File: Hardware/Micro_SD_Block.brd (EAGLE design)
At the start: 30.5 x 44.5 mm, 16 parts, among them U1 USD-SOCKETNEW, U2 EDISON_CONNECTOR_FULLMOUNTING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, U3 EDISON_CONNECTOR_FULLHEADER

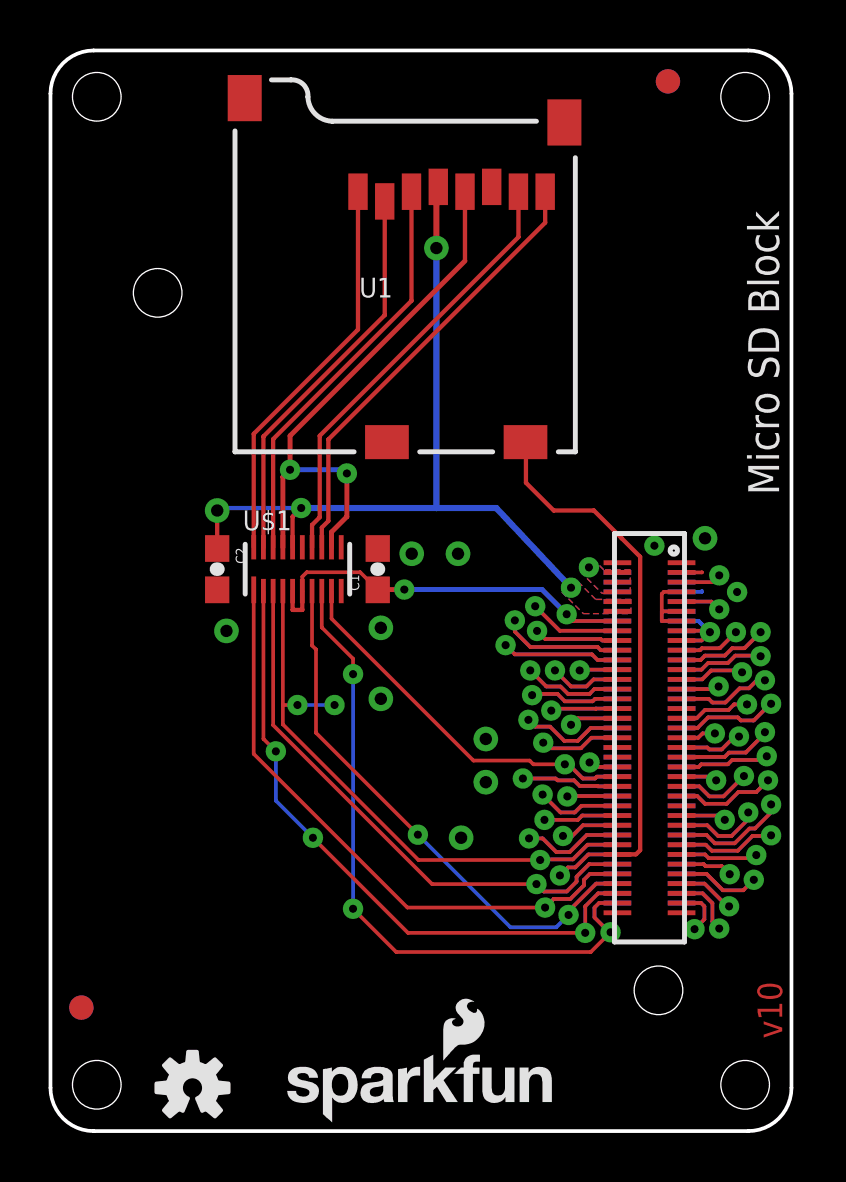
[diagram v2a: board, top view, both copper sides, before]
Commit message: Moved 3.3v bus out from under highspeed lines updated edison connector footprint to remove jumpers removed jumpers from txb0108
TODO: Remove P$#'s from txb0108 in library
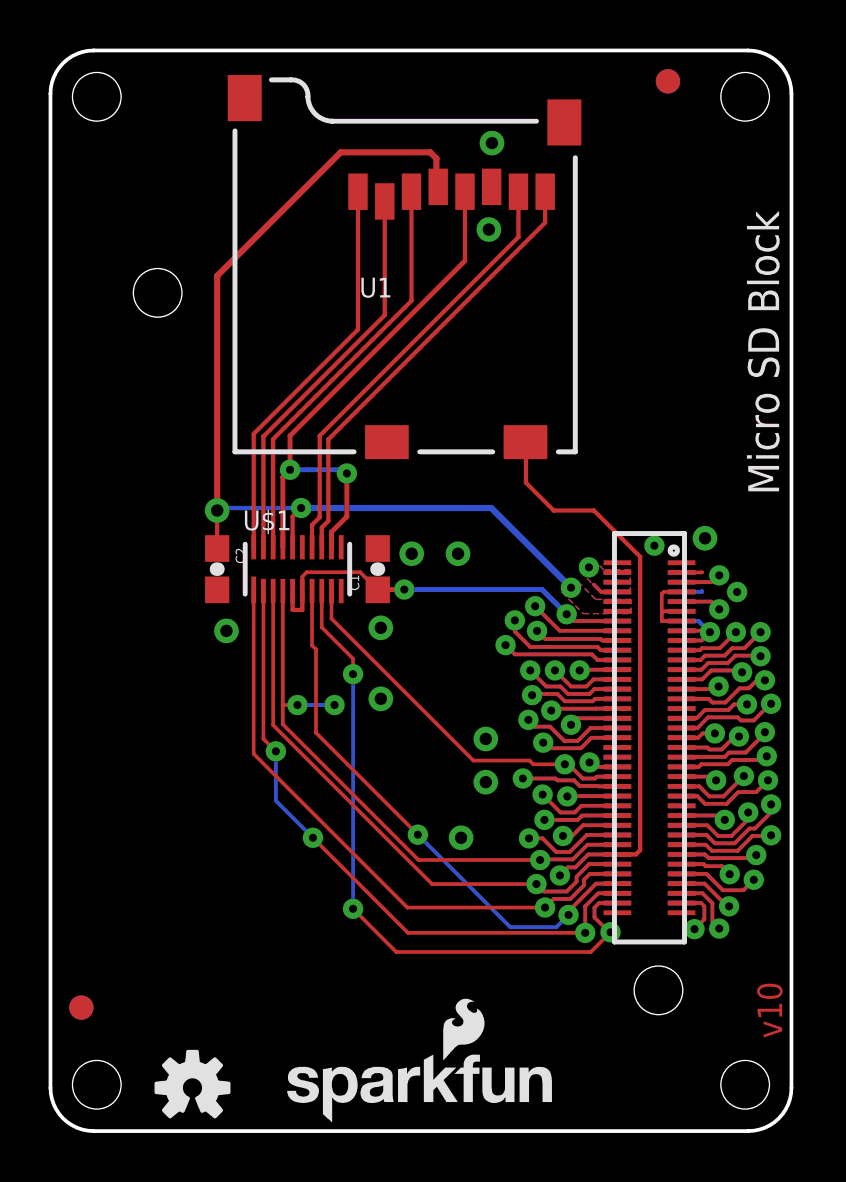
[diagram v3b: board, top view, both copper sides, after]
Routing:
- net 3.3V: track 32.6 -> 41.5 mm, vias 4 -> 3
- net VSYS: track 0.00 -> 2.18 mm
- net GND: vias 12 -> 14
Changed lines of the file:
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@@
 <layers>
 <layer number="1" name="Top" color="4" fill="1" visible="yes" active="yes"/>
-<layer number="2" name="Route2" color="1" fill="3" visible="yes" active="yes"/>
-<layer number="15" name="Route15" color="4" fill="6" visible="yes" active="yes"/>
+<layer number="2" name="Route2" color="1" fill="3" visible="no" active="yes"/>
+<layer number="15" name="Route15" color="4" fill="6" visible="no" active="yes"/>
 <layer number="16" name="Bottom" color="1" fill="1" visible="yes" active="yes"/>
 <layer number="17" name="Pads" color="2" fill="1" visible="yes" active="yes"/>
@@
 <layer number="21" name="tPlace" color="16" fill="1" visible="yes" active="yes"/>
 <layer number="22" name="bPlace" color="14" fill="1" visible="yes" active="yes"/>
-<layer number="23" name="tOrigins" color="15" fill="1" visible="yes" active="yes"/>
-<layer number="24" name="bOrigins" color="15" fill="1" visible="yes" active="yes"/>
-<layer number="25" name="tNames" color="7" fill="1" visible="yes" active="yes"/>
-<layer number="26" name="bNames" color="7" fill="1" visible="yes" active="yes"/>
-<layer number="27" name="tValues" color="7" fill="1" visible="yes" active="yes"/>
-<layer number="28" name="bValues" color="7" fill="1" visible="yes" active="yes"/>
-<layer number="29" name="tStop" color="7" fill="3" visible="yes" active="yes"/>
-<layer number="30" name="bStop" color="7" fill="6" visible="yes" active="yes"/>
-<layer number="31" name="tCream" color="7" fill="4" visible="yes" active="yes"/>
-<layer number="32" name="bCream" color="7" fill="5" visible="yes" active="yes"/>
-<layer number="39" name="tKeepout" color="4" fill="11" visible="yes" active="yes"/>
-<layer number="40" name="bKeepout" color="1" fill="11" visible="yes" active="yes"/>
-<layer number="41" name="tRestrict" color="4" fill="10" visible="yes" active="yes"/>
-<layer number="42" name="bRestrict" color="1" fill="10" visible="yes" active="yes"/>
-<layer number="43" name="vRestrict" color="2" fill="10" visible="yes" active="yes"/>
-<layer number="44" name="Drills" color="7" fill="1" visible="yes" active="yes"/>
-<layer number="45" name="Holes" color="7" fill="1" visible="yes" active="yes"/>
-<layer number="46" name="Milling" color="3" fill="1" visible="yes" active="yes"/>
-<layer number="51" name="tDocu" color="6" fill="1" visible="yes" active="yes"/>
+<layer number="23" name="tOrigins" color="15" fill="1" visible="no" active="yes"/>
+<layer number="24" name="bOrigins" color="15" fill="1" visible="no" active="yes"/>
+<layer number="25" name="tNames" color="7" fill="1" visible="no" active="yes"/>
+<layer number="26" name="bNames" color="7" fill="1" visible="no" active="yes"/>
+<layer number="27" name="tValues" color="7" fill="1" visible="no" active="yes"/>
+<layer number="28" name="bValues" color="7" fill="1" visible="no" active="yes"/>
+<layer number="29" name="tStop" color="7" fill="3" visible="no" active="yes"/>
+<layer number="30" name="bStop" color="7" fill="6" visible="no" active="yes"/>
+<layer number="31" name="tCream" color="7" fill="4" visible="no" active="yes"/>
+<layer number="32" name="bCream" color="7" fill="5" visible="no" active="yes"/>
+<layer number="39" name="tKeepout" color="4" fill="11" visible="no" active="yes"/>
+<layer number="40" name="bKeepout" color="1" fill="11" visible="no" active="yes"/>
+<layer number="41" name="tRestrict" color="4" fill="10" visible="no" active="yes"/>
+<layer number="42" name="bRestrict" color="1" fill="10" visible="no" active="yes"/>
+<layer number="43" name="vRestrict" color="2" fill="10" visible="no" active="yes"/>
+<layer number="44" name="Drills" color="7" fill="1" visible="no" active="yes"/>
+<layer number="45" name="Holes" color="7" fill="1" visible="no" active="yes"/>
+<layer number="46" name="Milling" color="3" fill="1" visible="no" active="yes"/>
+<layer number="51" name="tDocu" color="6" fill="1" visible="no" active="yes"/>
 <layer number="3" name="Route3" color="4" fill="3" visible="no" active="no"/>
 <layer number="4" name="Route4" color="1" fill="4" visible="no" active="no"/>
@@
 <layer number="251" name="SMDround" color="12" fill="11" visible="no" active="no"/>
 <layer number="254" name="cooling" color="7" fill="1" visible="no" active="no"/>
-<layer number="255" name="routoute" color="7" fill="1" visible="yes" active="yes"/>
+<layer number="255" name="routoute" color="7" fill="1" visible="no" active="yes"/>
 </layers>
 <board>
@@
 <signals>
 <signal name="GND">
-<polygon width="0.1778" layer="16" spacing="0.254" isolate="0.0508" rank="6">
+<polygon width="0.1524" layer="16" spacing="0.254" isolate="0.0508" rank="6">
 <vertex x="30.48" y="42.672"/>
 <vertex x="30.48" y="1.778" curve="-90"/>
@@
 <via x="17.907" y="16.129" extent="1-16" drill="0.508"/>
 <via x="13.589" y="20.701" extent="1-16" drill="0.508"/>
+<via x="18.034" y="37.084" extent="1-16" drill="0.508"/>
+<via x="18.161" y="40.64" extent="1-16" drill="0.508"/>
 </signal>
 <signal name="VSYS">
@@
 <vertex x="21.7932" y="23.0124"/>
 </polygon>
+<wire x1="23.32" y1="22.18" x2="22.651" y2="22.18" width="0.1524" layer="16"/>
+<wire x1="22.651" y1="22.18" x2="22.352" y2="22.479" width="0.1524" layer="16"/>
+<wire x1="23.32" y1="22.1798" x2="22.6512" y2="22.1798" width="0.1524" layer="1"/>
+<wire x1="22.6512" y1="22.1798" x2="22.352" y2="22.479" width="0.1524" layer="1"/>
 </signal>
 <signal name="3.3V">
@@
 <wire x1="9.96" y1="24.014" x2="9.96" y2="25.2762" width="0.1778" layer="1"/>
 <wire x1="9.96" y1="25.2762" x2="10.3124" y2="25.6286" width="0.1778" layer="1"/>
-<via x="15.875" y="36.322" extent="1-16" drill="0.508"/>
 <contactref element="C2" pad="1"/>
 <wire x1="6.858" y1="23.964" x2="6.858" y2="25.527" width="0.1778" layer="1"/>
@@
 <wire x1="6.9596" y1="25.6286" x2="10.3124" y2="25.6286" width="0.1778" layer="16"/>
 <via x="21.4122" y="22.352" extent="1-16" drill="0.3302"/>
-<wire x1="21.4122" y1="22.352" x2="18.3388" y2="25.6286" width="0.254" layer="16"/>
-<wire x1="18.3388" y1="25.6286" x2="15.875" y2="25.6286" width="0.254" layer="16"/>
-<wire x1="15.875" y1="25.6286" x2="10.3124" y2="25.6286" width="0.254" layer="16"/>
-<wire x1="15.875" y1="36.322" x2="15.875" y2="25.6286" width="0.254" layer="16"/>
-<wire x1="15.875" y1="36.322" x2="15.875" y2="38.765" width="0.254" layer="1"/>
+<wire x1="18.1356" y1="25.6286" x2="10.3124" y2="25.6286" width="0.254" layer="16"/>
 <wire x1="15.875" y1="38.765" x2="15.95" y2="38.84" width="0.254" layer="1"/>
 <polygon width="0.1524" layer="1" isolate="0.0508">
@@
 <vertex x="21.9202" y="21.2852"/>
 </polygon>
+<wire x1="18.1356" y1="25.6286" x2="21.4122" y2="22.352" width="0.254" layer="16"/>
+<wire x1="15.875" y1="38.765" x2="15.875" y2="40.005" width="0.254" layer="1"/>
+<wire x1="15.875" y1="40.005" x2="15.621" y2="40.259" width="0.254" layer="1"/>
+<wire x1="15.621" y1="40.259" x2="11.938" y2="40.259" width="0.254" layer="1"/>
+<wire x1="11.938" y1="40.259" x2="6.858" y2="35.179" width="0.254" layer="1"/>
+<wire x1="6.858" y1="35.179" x2="6.858" y2="25.527" width="0.254" layer="1"/>
 </signal>
 <signal name="GP183_PWM3">
@@
 <wire x1="22.353" y1="25.527" x2="20.701" y2="25.527" width="0.1778" layer="1"/>
 <wire x1="20.701" y1="25.527" x2="19.558" y2="26.67" width="0.1778" layer="1"/>
-<wire x1="19.558" y1="26.67" x2="19.558" y2="28.321" width="0.1778" layer="1"/>
-<wire x1="19.558" y1="28.321" x2="19.54" y2="28.34" width="0.1778" layer="1"/>
+<wire x1="19.558" y1="26.67" x2="19.558" y2="28.322" width="0.1778" layer="1"/>
+<wire x1="19.558" y1="28.322" x2="19.54" y2="28.34" width="0.1778" layer="1"/>
 </signal>
 <signal name="GP79_SD_0_CMD">
